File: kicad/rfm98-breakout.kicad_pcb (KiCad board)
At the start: 2 copper layers, 29 x 24 mm, 26 parts

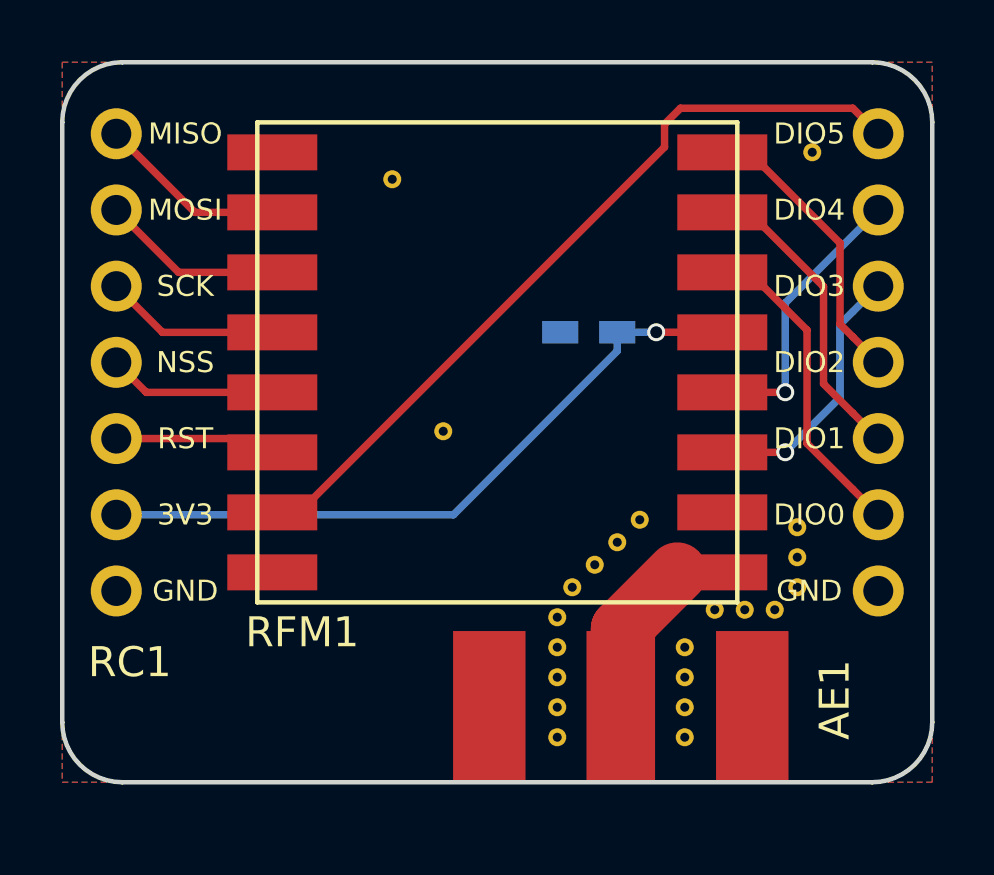
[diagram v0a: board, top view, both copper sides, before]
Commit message: rotated rf module
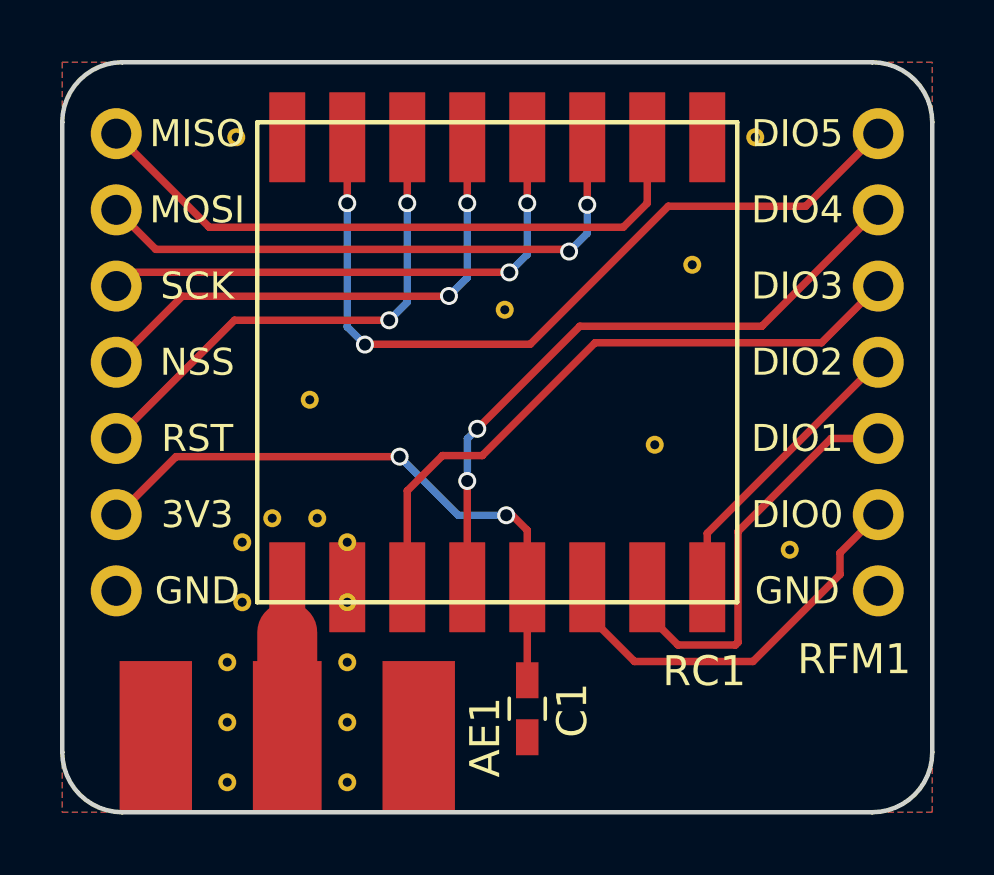
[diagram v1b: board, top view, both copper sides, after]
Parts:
- removed the REF** at (158.5, 110.5)
- removed the REF** at (150.5, 116.5)
- removed the REF** at (150.5, 115.5)
- removed the REF** at (150.5, 114.5)
- removed the REF** at (155.8, 113.2)
- removed the REF** at (154.8, 114.5)
- removed the REF** at (151.8, 111.8)
- removed the REF** at (150.5, 113.5)
- removed the REF** at (151.0, 112.5)
- removed the REF** at (152.5, 111.0)
- removed the REF** at (153.2, 110.2)
- removed the REF** at (158.5, 111.5)
- removed the REF** at (159.0, 98.0)
- removed the REF** at (146.7, 107.3)
- removed the REF** at (145.0, 98.9)
- removed the REF** at (158.5, 112.5)
- removed the REF** at (157.8, 113.2)
- removed the REF** at (156.8, 113.2)
- removed the REF** at (154.8, 117.5)
- removed the REF** at (154.8, 116.5)
- removed the REF** at (154.8, 115.5)
- removed the REF** at (150.5, 117.5)
- added REF**: STITCHING_VIA, utils:STITCHING_VIA, F.Cu at (158.2, 111.2)
- added REF**: STITCHING_VIA, utils:STITCHING_VIA, F.Cu at (140.0, 111.0)
- added REF**: STITCHING_VIA, utils:STITCHING_VIA, F.Cu at (140.0, 113.0)
- added REF**: STITCHING_VIA, utils:STITCHING_VIA, F.Cu at (139.5, 115.0)
- added REF**: STITCHING_VIA, utils:STITCHING_VIA, F.Cu at (139.5, 117.0)
- added REF**: STITCHING_VIA, utils:STITCHING_VIA, F.Cu at (143.5, 115.0)
- added REF**: STITCHING_VIA, utils:STITCHING_VIA, F.Cu at (143.5, 117.0)
- added REF**: STITCHING_VIA, utils:STITCHING_VIA, F.Cu at (143.5, 119.0)
- added REF**: STITCHING_VIA, utils:STITCHING_VIA, F.Cu at (139.5, 119.0)
- added REF**: STITCHING_VIA, utils:STITCHING_VIA, F.Cu at (139.8, 97.5)
- added REF**: STITCHING_VIA, utils:STITCHING_VIA, F.Cu at (157.1, 97.5)
- added REF**: STITCHING_VIA, utils:STITCHING_VIA, F.Cu at (148.8, 103.2)
- added REF**: STITCHING_VIA, utils:STITCHING_VIA, F.Cu at (153.8, 107.8)
- added REF**: STITCHING_VIA, utils:STITCHING_VIA, F.Cu at (155.0, 101.8)
- added REF**: STITCHING_VIA, utils:STITCHING_VIA, F.Cu at (142.2, 106.2)
- added REF**: STITCHING_VIA, utils:STITCHING_VIA, F.Cu at (143.5, 111.0)
- added REF**: STITCHING_VIA, utils:STITCHING_VIA, F.Cu at (143.5, 113.0)
- added REF**: STITCHING_VIA, utils:STITCHING_VIA, F.Cu at (142.5, 110.2)
- added REF**: STITCHING_VIA, utils:STITCHING_VIA, F.Cu at (141.0, 110.2)
- C1: moved to F.Cu
- moved C1 12.7 mm to (149.5, 116.5), turned to 270 degrees
- moved AE1 11.2 mm to (141.5, 117.5)
- turned RFM1 to 270 degrees
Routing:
- net Net-(RC1-Pad1): track 7.19 -> 21.5 mm
- net Net-(RC1-Pad2): track 6.64 -> 19.7 mm, vias 0 -> 2
- net Net-(RC1-Pad11): track 8.92 -> 21.7 mm, vias 1 -> 0
- net Net-(RC1-Pad12): track 9.46 -> 21.8 mm, vias 1 -> 2
- net Net-(RC1-Pad3): track 5.84 -> 18.0 mm, vias 0 -> 2
- net Net-(RC1-Pad4): track 5.61 -> 17.5 mm, vias 0 -> 2
- net Net-(RC1-Pad5): track 5.39 -> 17.1 mm, vias 0 -> 2
- net Net-(RC1-Pad9): track 10.2 -> 14.0 mm
- net Net-(RC1-Pad8): track 10.8 -> 13.7 mm
- net Net-(C1-Pad1): track 23.1 -> 20.5 mm, vias 1 -> 2
- net Net-(AE1-Pad1): track 5.28 -> 3.25 mm
- net Net-(RC1-Pad13): track 26.6 -> 27.2 mm, vias 0 -> 2
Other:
- board size 29 x 24 mm -> 29 x 25 mm
- board text added: "hochreiner.net rfm98-breakout V1.0.1"
- board text removed: "hochreiner.net rfm98-breakout V1.0.0"
